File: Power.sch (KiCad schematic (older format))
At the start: 14 parts

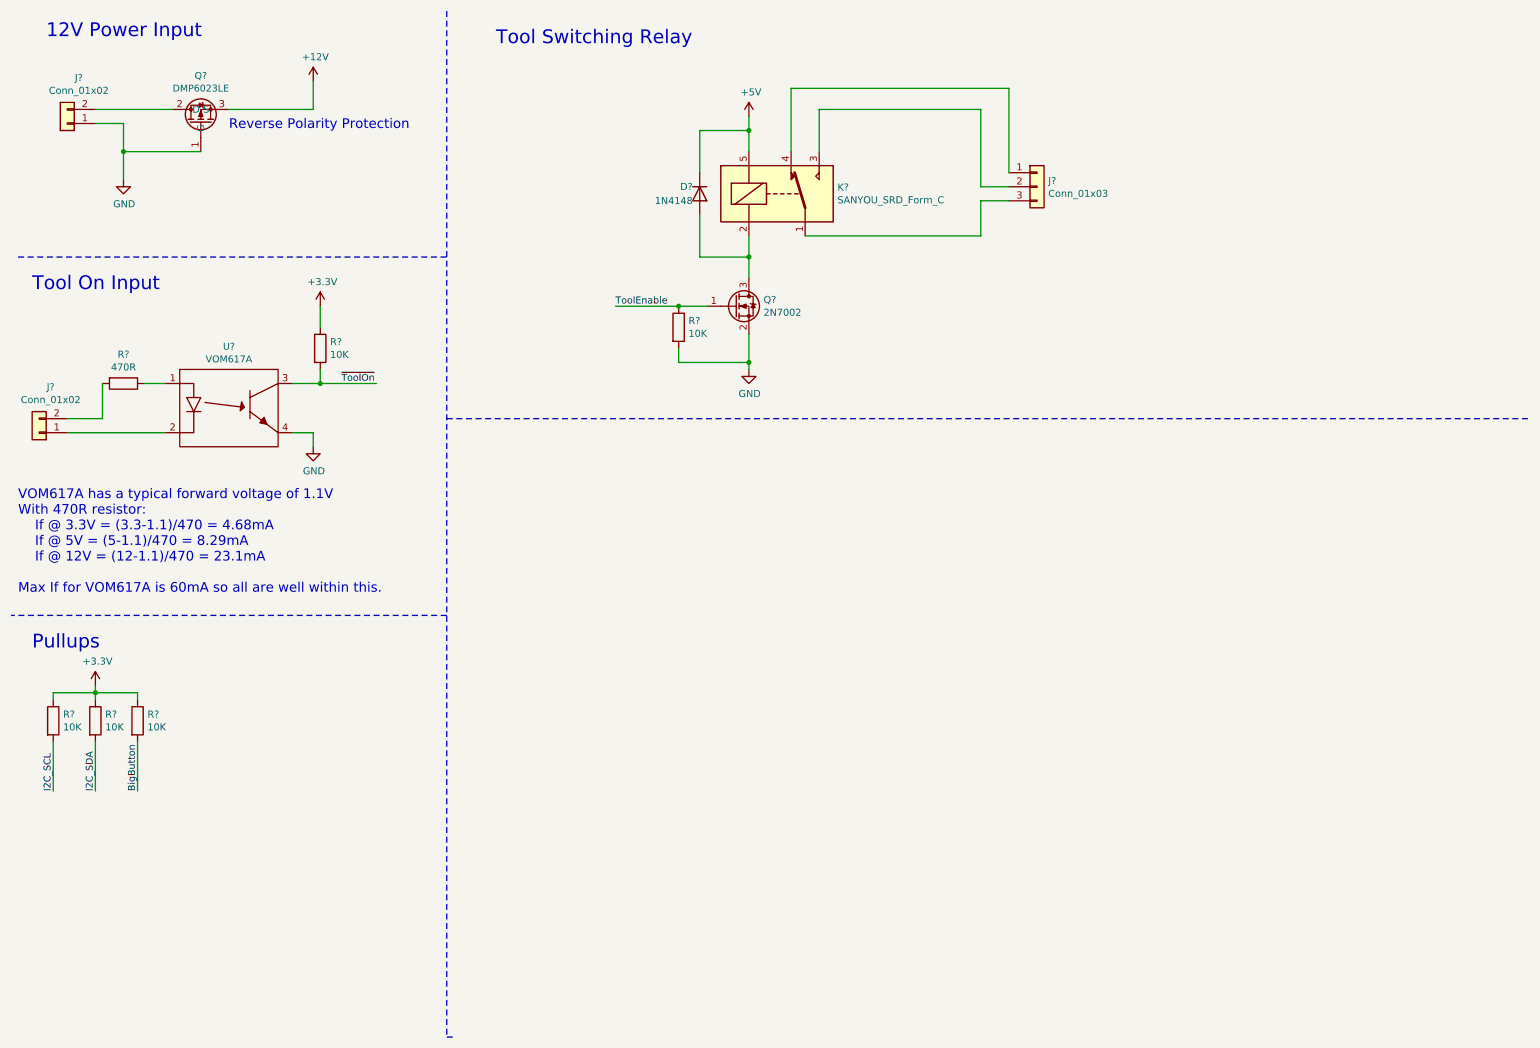
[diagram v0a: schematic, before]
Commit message: Annotated some symbols and linked nets properly between sheets
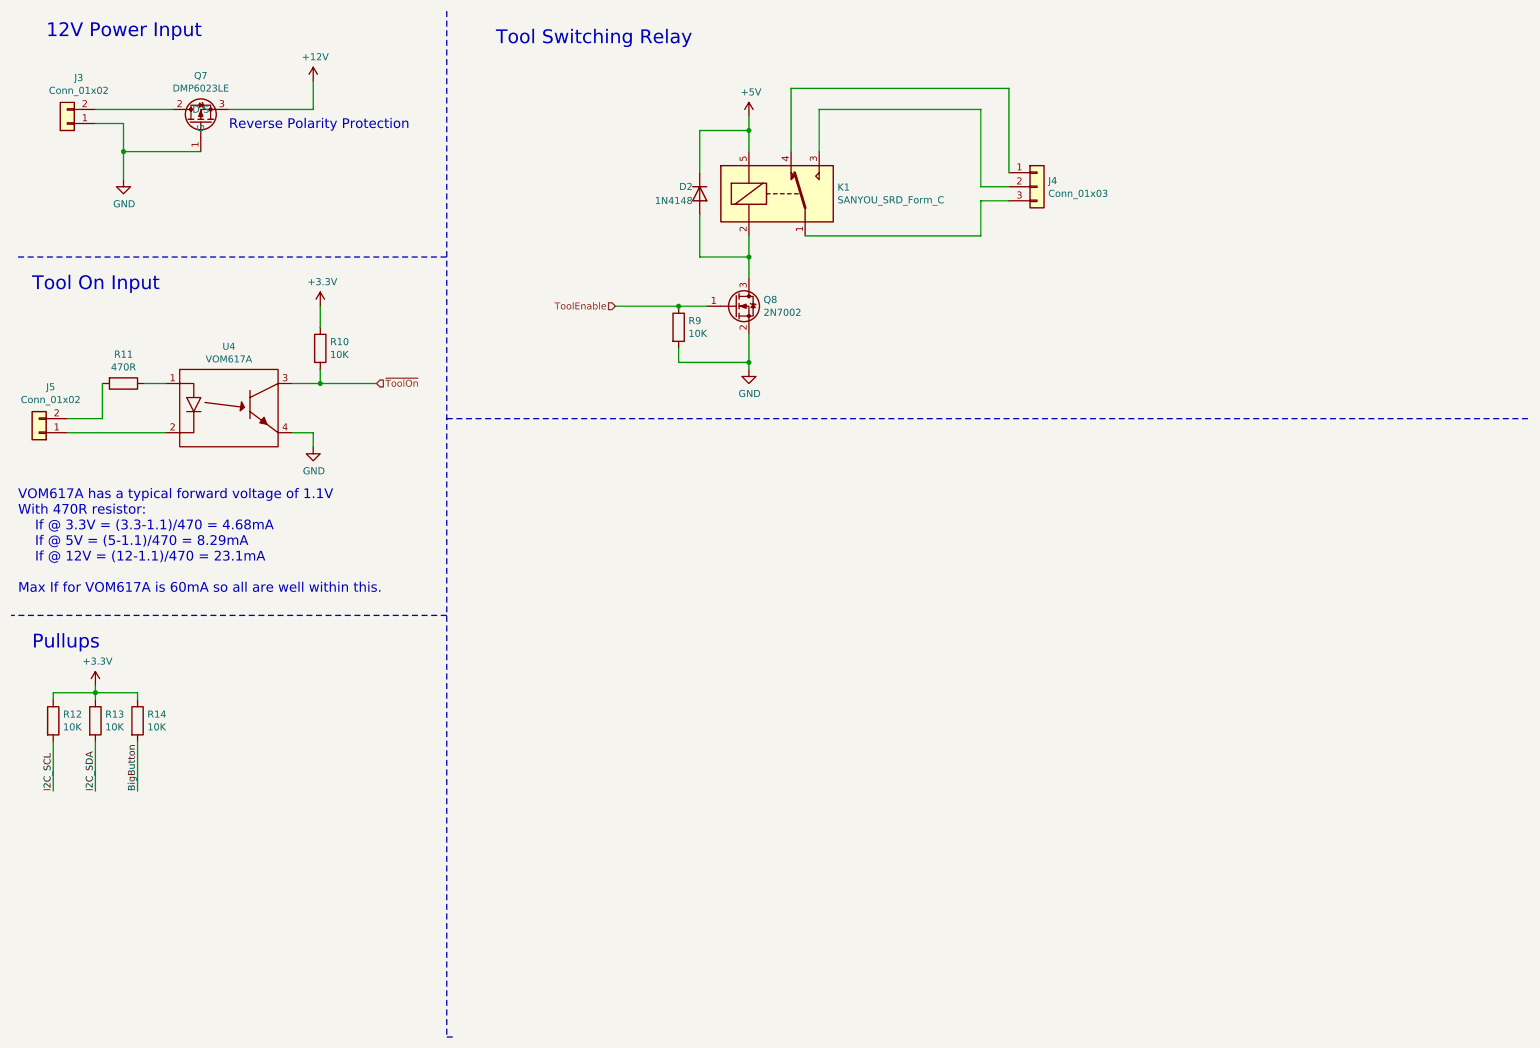
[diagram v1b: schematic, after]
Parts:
- J3: renamed from J?; footprint (none) -> ExtraParts:Connector-5.08mm
- R10, R11, R12, R13, R14, R9: renamed from R?; footprint (none) -> Resistor_SMD:R_0603_1608Metric
- gave numbers to parts that had none: 7
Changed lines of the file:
@@
 $EndDescr
 $Comp
-L Connector_Generic:Conn_01x02 J?
+L Connector_Generic:Conn_01x02 J3
 U 1 1 5FFEA204
 P 850 1300
-F 0 "J?" H 768 975 50  0000 C CNN
+F 0 "J3" H 768 975 50  0000 C CNN
 F 1 "Conn_01x02" H 768 1066 50  0000 C CNN
-F 2 "" H 850 1300 50  0001 C CNN
+F 2 "ExtraParts:Connector-5.08mm" H 850 1300 50  0001 C CNN
 F 3 "~" H 850 1300 50  0001 C CNN
 	1    850  1300
@@
 $EndComp
 $Comp
-L ExtraParts:DMP6023LE Q?
+L ExtraParts:DMP6023LE Q7
 U 1 1 5FFEE310
 P 1800 1250
-F 0 "Q?" V 2090 1250 49  0000 C CNN
+F 0 "Q7" V 2090 1250 49  0000 C CNN
 F 1 "DMP6023LE" V 2000 1250 49  0000 C CNN
 F 2 "Package_TO_SOT_SMD:SOT-223" H 1950 1400 49  0001 L CNN
@@
 	500  2250 3550 2250
 $Comp
-L Relay:SANYOU_SRD_Form_C K?
+L Relay:SANYOU_SRD_Form_C K1
 U 1 1 5FFFB5FD
 P 5900 1800
-F 0 "K?" H 6330 1846 50  0000 L CNN
+F 0 "K1" H 6330 1846 50  0000 L CNN
 F 1 "SANYOU_SRD_Form_C" H 6330 1755 50  0000 L CNN
 F 2 "Relay_THT:Relay_SPDT_SANYOU_SRD_Series_Form_C" H 6350 1750 50  0001 L CNN
@@
 $EndComp
 $Comp
-L Transistor_FET:2N7002 Q?
+L Transistor_FET:2N7002 Q8
 U 1 1 60000340
 P 5600 2600
-F 0 "Q?" H 5804 2646 50  0000 L CNN
+F 0 "Q8" H 5804 2646 50  0000 L CNN
 F 1 "2N7002" H 5804 2555 50  0000 L CNN
 F 2 "Package_TO_SOT_SMD:SOT-23" H 5800 2525 50  0001 L CIN
@@
 	5700 1500 5700 1350
 $Comp
-L Device:R R?
+L Device:R R9
 U 1 1 60004E1E
 P 5200 2750
-F 0 "R?" H 5270 2796 50  0000 L CNN
+F 0 "R9" H 5270 2796 50  0000 L CNN
 F 1 "10K" H 5270 2705 50  0000 L CNN
-F 2 "" V 5130 2750 50  0001 C CNN
+F 2 "Resistor_SMD:R_0603_1608Metric" V 5130 2750 50  0001 C CNN
 F 3 "~" H 5200 2750 50  0001 C CNN
 	1    5200 2750
@@
 Wire Wire Line
 	5700 3000 5700 2800
-Text Label 4750 2600 0    49   ~ 0
-ToolEnable
 Wire Wire Line
 	5200 2600 4750 2600
 Connection ~ 5200 2600
 $Comp
-L Connector_Generic:Conn_01x03 J?
+L Connector_Generic:Conn_01x03 J4
 U 1 1 60006F53
 P 7750 1750
-F 0 "J?" H 7830 1792 50  0000 L CNN
+F 0 "J4" H 7830 1792 50  0000 L CNN
 F 1 "Conn_01x03" H 7830 1701 50  0000 L CNN
 F 2 "" H 7750 1750 50  0001 C CNN
@@
 	7350 1750 7550 1750
 $Comp
-L Diode:1N4148 D?
+L Diode:1N4148 D2
 U 1 1 60009065
 P 5350 1800
-F 0 "D?" V 5300 1750 50  0000 R CNN
+F 0 "D2" V 5300 1750 50  0000 R CNN
 F 1 "1N4148" V 5400 1750 50  0000 R CNN
 F 2 "Diode_THT:D_DO-35_SOD27_P7.62mm_Horizontal" H 5350 1625 50  0001 C CNN
@@
 Tool On Input
 $Comp
-L ExtraParts:VOM617A U?
+L ExtraParts:VOM617A U4
 U 1 1 6003FB1A
 P 2000 3300
-F 0 "U?" H 2000 3713 49  0000 C CNN
+F 0 "U4" H 2000 3713 49  0000 C CNN
 F 1 "VOM617A" H 2000 3623 49  0000 C CNN
 F 2 "" H 2000 3300 49  0001 C CNN
@@
 $EndComp
 $Comp
-L Device:R R?
+L Device:R R11
 U 1 1 60040FCE
 P 1250 3150
-F 0 "R?" V 1043 3150 50  0000 C CNN
+F 0 "R11" V 1043 3150 50  0000 C CNN
 F 1 "470R" V 1134 3150 50  0000 C CNN
-F 2 "" V 1180 3150 50  0001 C CNN
+F 2 "Resistor_SMD:R_0603_1608Metric" V 1180 3150 50  0001 C CNN
 F 3 "~" H 1250 3150 50  0001 C CNN
 	1    1250 3150
@@
 $EndComp
 $Comp
-L Connector_Generic:Conn_01x02 J?
+L Connector_Generic:Conn_01x02 J5
 U 1 1 600418EE
 P 650 3500
-F 0 "J?" H 568 3175 50  0000 C CNN
+F 0 "J5" H 568 3175 50  0000 C CNN
 F 1 "Conn_01x02" H 568 3266 50  0000 C CNN
 F 2 "" H 650 3500 50  0001 C CNN
@@
 	2600 3500 2600 3600
 $Comp
-L Device:R R?
+L Device:R R10
 U 1 1 60048EFA
 P 2650 2900
-F 0 "R?" H 2720 2946 50  0000 L CNN
+F 0 "R10" H 2720 2946 50  0000 L CNN
 F 1 "10K" H 2720 2855 50  0000 L CNN
-F 2 "" V 2580 2900 50  0001 C CNN
+F 2 "Resistor_SMD:R_0603_1608Metric" V 2580 2900 50  0001 C CNN
 F 3 "~" H 2650 2900 50  0001 C CNN
 	1    2650 2900
@@
 Wire Wire Line
 	2650 3150 2450 3150
-Text Label 2800 3150 0    49   ~ 0
-~ToolOn
 Wire Wire Line
 	2650 3150 3050 3150
@@
 Pullups
 $Comp
-L Device:R R?
+L Device:R R12
 U 1 1 600D6942
 P 750 5550
-F 0 "R?" H 820 5596 50  0000 L CNN
+F 0 "R12" H 820 5596 50  0000 L CNN
 F 1 "10K" H 820 5505 50  0000 L CNN
-F 2 "" V 680 5550 50  0001 C CNN
+F 2 "Resistor_SMD:R_0603_1608Metric" V 680 5550 50  0001 C CNN
 F 3 "~" H 750 5550 50  0001 C CNN
 	1    750  5550
@@
 $EndComp
 $Comp
-L Device:R R?
+L Device:R R13
 U 1 1 600D76CA
 P 1050 5550
-F 0 "R?" H 1120 5596 50  0000 L CNN
+F 0 "R13" H 1120 5596 50  0000 L CNN
 F 1 "10K" H 1120 5505 50  0000 L CNN
-F 2 "" V 980 5550 50  0001 C CNN
+F 2 "Resistor_SMD:R_0603_1608Metric" V 980 5550 50  0001 C CNN
 F 3 "~" H 1050 5550 50  0001 C CNN
 	1    1050 5550
@@
 $EndComp
 $Comp
-L power:+3.3V #PWR?
+L power:+3.3V #PWR01
 U 1 1 600D7C56
 P 1050 5300
-F 0 "#PWR?" H 1050 5150 50  0001 C CNN
+F 0 "#PWR01" H 1050 5150 50  0001 C CNN
 F 1 "+3.3V" H 1065 5473 50  0000 C CNN
 F 2 "" H 1050 5300 50  0001 C CNN
@@
 	1050 5400 1050 5350
 $Comp
-L Device:R R?
+L Device:R R14
 U 1 1 600F2ACB
 P 1350 5550
-F 0 "R?" H 1420 5596 50  0000 L CNN
+F 0 "R14" H 1420 5596 50  0000 L CNN
 F 1 "10K" H 1420 5505 50  0000 L CNN
-F 2 "" V 1280 5550 50  0001 C CNN
+F 2 "Resistor_SMD:R_0603_1608Metric" V 1280 5550 50  0001 C CNN
 F 3 "~" H 1350 5550 50  0001 C CNN
 	1    1350 5550
@@
 Wire Wire Line
 	1050 5350 1050 5300
+Text HLabel 4750 2600 0    49   Input ~ 0
+ToolEnable
+Text HLabel 3050 3150 2    49   Input ~ 0
+~ToolOn
 $EndSCHEMATC

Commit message: First pass at routing board fully
Also fixed a stupid error on the Nucleo-144 footprint
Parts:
- J4: footprint (none) -> ExtraParts:Connector-3.81mm-3pin
- J5: footprint (none) -> ExtraParts:Connector-3.81mm-2pin
- U4: footprint (none) -> ExtraParts:VOM617A-4SOP
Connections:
- net at K1.1: now also J4.2 (Pin_2); no longer J4.3 (Pin_3)
- net at K1.3: now also J4.1 (Pin_1); no longer J4.2 (Pin_2)
- net at K1.4: now also J4.3 (Pin_3); no longer J4.1 (Pin_1)
- net at U4.2: now also J5.2 (Pin_2); no longer J5.1 (Pin_1)
- net at R11.2: now also J5.1 (Pin_1); no longer J5.2 (Pin_2)
- net I2C_SCL renamed i2c_SCL
- net I2C_SDA renamed i2c_SDA
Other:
- moved on the sheet: J4
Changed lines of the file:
@@
 L Connector_Generic:Conn_01x03 J4
 U 1 1 60006F53
-P 7750 1750
-F 0 "J4" H 7830 1792 50  0000 L CNN
-F 1 "Conn_01x03" H 7830 1701 50  0000 L CNN
-F 2 "" H 7750 1750 50  0001 C CNN
-F 3 "~" H 7750 1750 50  0001 C CNN
-	1    7750 1750
-	1    0    0    -1
-$EndComp
-Wire Wire Line
-	6100 2100 7350 2100
-Wire Wire Line
-	7350 2100 7350 1850
-Wire Wire Line
-	7350 1850 7550 1850
-Wire Wire Line
-	7550 1650 7550 1050
-Wire Wire Line
-	7550 1050 6000 1050
-Wire Wire Line
-	6000 1050 6000 1500
-Wire Wire Line
-	6200 1500 6200 1200
-Wire Wire Line
-	6200 1200 7350 1200
-Wire Wire Line
-	7350 1200 7350 1750
-Wire Wire Line
-	7350 1750 7550 1750
+P 6100 900
+F 0 "J4" V 6064 1080 50  0000 L CNN
+F 1 "Conn_01x03" V 5973 1080 50  0000 L CNN
+F 2 "ExtraParts:Connector-3.81mm-3pin" H 6100 900 50  0001 C CNN
+F 3 "~" H 6100 900 50  0001 C CNN
+	1    6100 900
+	0    1    -1   0
+$EndComp
 $Comp
 L Diode:1N4148 D2
@@
 F 0 "U4" H 2000 3713 49  0000 C CNN
 F 1 "VOM617A" H 2000 3623 49  0000 C CNN
-F 2 "" H 2000 3300 49  0001 C CNN
+F 2 "ExtraParts:VOM617A-4SOP" H 2000 3300 49  0001 C CNN
 F 3 "https://www.vishay.com/docs/83446/vom617a.pdf" H 2000 3300 49  0001 C CNN
 	1    2000 3300
@@
 L Connector_Generic:Conn_01x02 J5
 U 1 1 600418EE
-P 650 3500
-F 0 "J5" H 568 3175 50  0000 C CNN
-F 1 "Conn_01x02" H 568 3266 50  0000 C CNN
-F 2 "" H 650 3500 50  0001 C CNN
-F 3 "~" H 650 3500 50  0001 C CNN
-	1    650  3500
-	-1   0    0    1
+P 650 3400
+F 0 "J5" H 568 3617 50  0000 C CNN
+F 1 "Conn_01x02" H 568 3526 50  0000 C CNN
+F 2 "ExtraParts:Connector-3.81mm-2pin" H 650 3400 50  0001 C CNN
+F 3 "~" H 650 3400 50  0001 C CNN
+	1    650  3400
+	-1   0    0    -1
 $EndComp
 Wire Wire Line
@@
 Text HLabel 3050 3150 2    49   Input ~ 0
 ~ToolOn
+Wire Wire Line
+	6000 1100 6000 1500
+Wire Wire Line
+	6200 1500 6200 1100
+Wire Wire Line
+	6100 1100 6100 1400
+Wire Wire Line
+	6100 1400 7200 1400
+Wire Wire Line
+	7200 1400 7200 2350
+Wire Wire Line
+	7200 2350 6100 2350
+Wire Wire Line
+	6100 2350 6100 2100
+Text GLabel 750  6050 3    49   Input ~ 0
+i2c_SCL
+Text GLabel 1050 6050 3    49   Input ~ 0
+i2c_SDA
+Text GLabel 1350 6050 3    49   Input ~ 0
+BigButton
 $EndSCHEMATC
